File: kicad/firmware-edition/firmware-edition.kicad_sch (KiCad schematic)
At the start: 103 parts, among them J1 Solar Panel, J10 GPIO, J12 GPIO, J13 SPI, J2 BATT, J3 3V3 Sensor Bus, J4 USB_C_Receptacle_USB2.0_16P, J5 I2C_3V3, J6 SWD, J7 Conn_01x01_Socket, J8 GPIO, J9 I2C_5V, Q1 BSS84, Q2 BSS84, Q3 BSS84, SW1 BOOT_DFU, SW2 RST, U1 ADP5091, U2 TPS61023DRLR, U3 MAX-M10M-00B, U4 Si4463, U5 STM32U073KCU6, Y1 30MHz

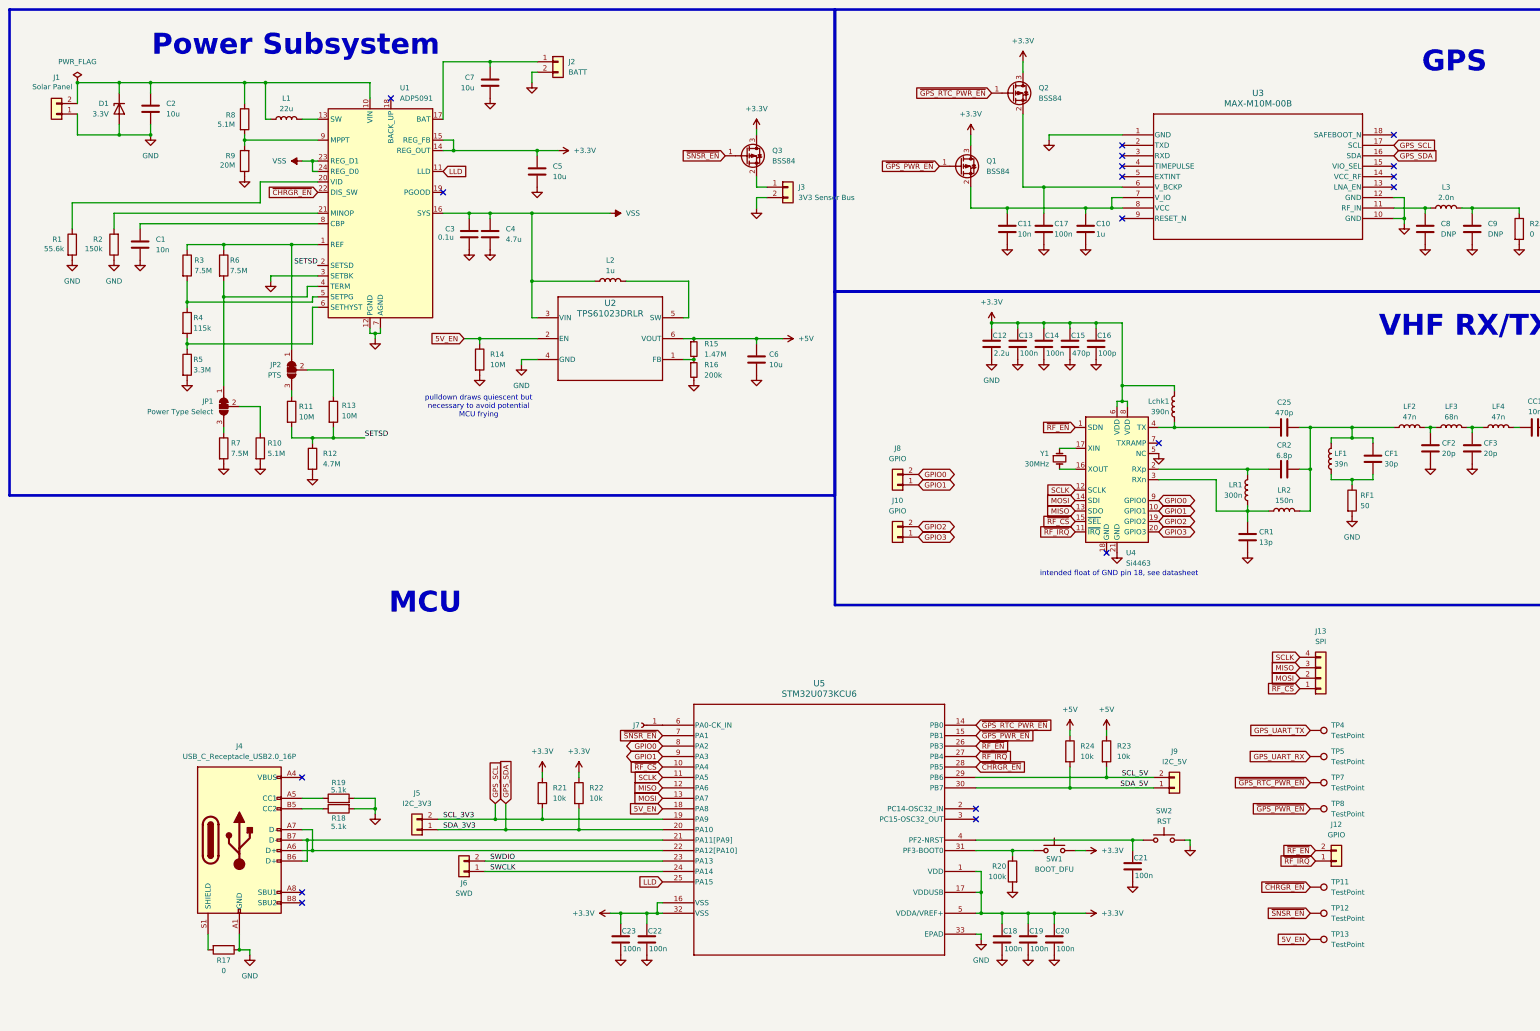
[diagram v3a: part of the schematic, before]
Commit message: PCB layout of System Board v1.01
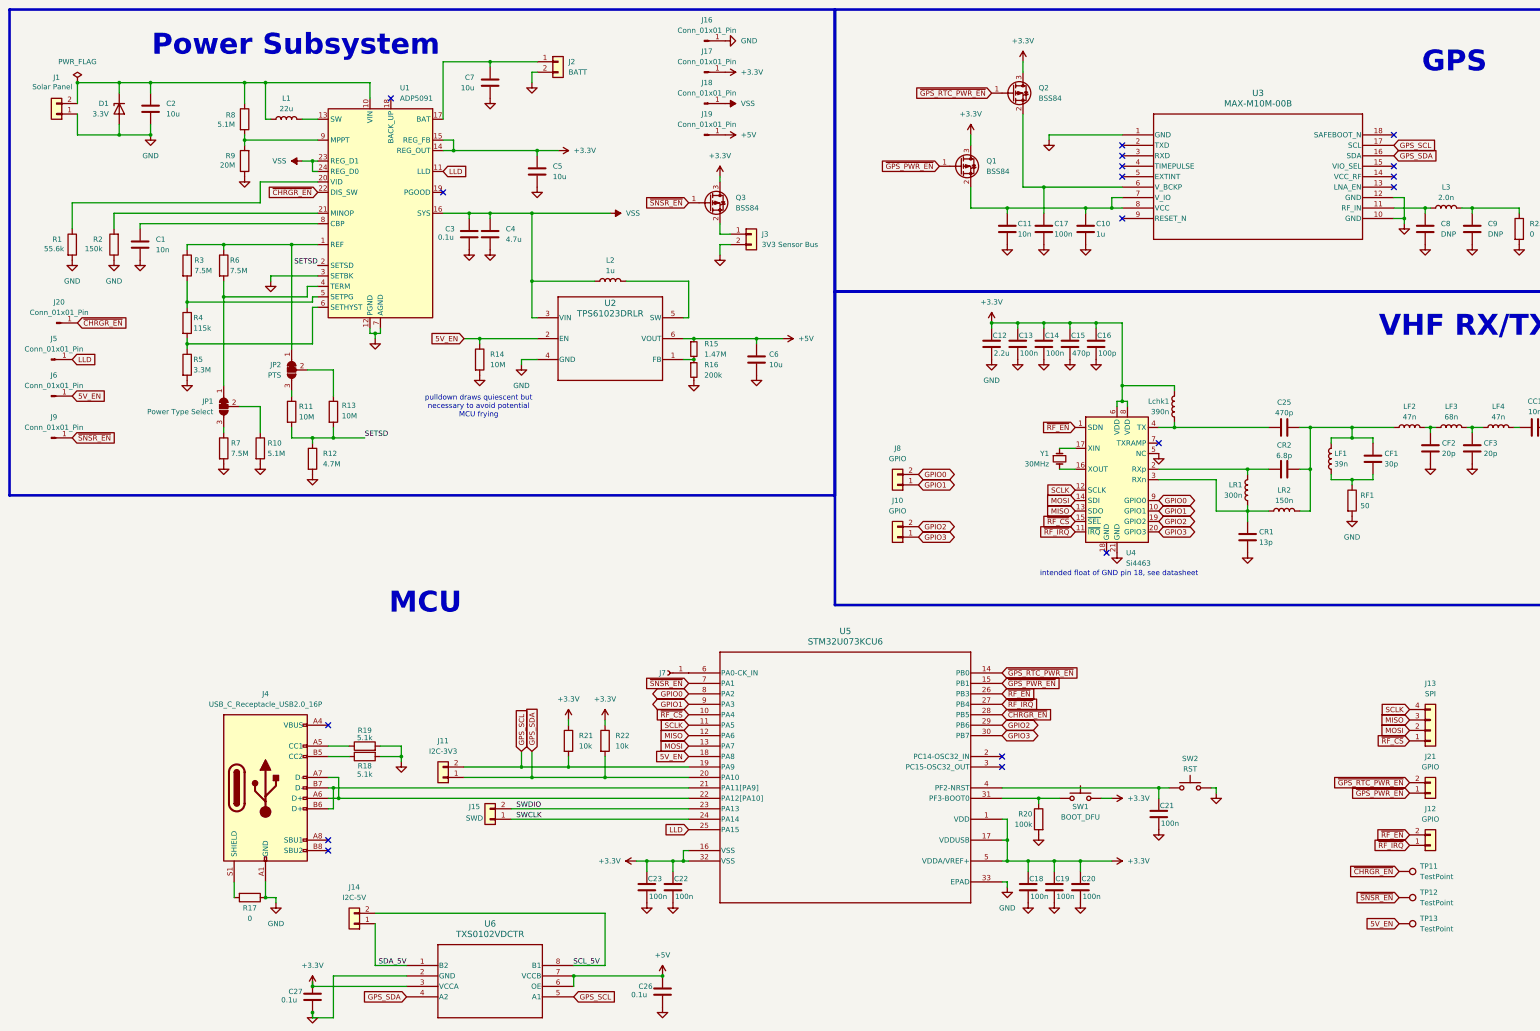
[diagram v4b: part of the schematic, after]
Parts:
- removed J5: I2C_3V3, symbol Connector_Generic:Conn_01x02
- removed J6: SWD, symbol Connector_Generic:Conn_01x02
- removed J9: I2C_5V, symbol Connector_Generic:Conn_01x02
- removed R23, R24: 10k, symbol Device:R
- removed TP4, TP5, TP7, TP8: TestPoint, symbol Connector:TestPoint
- added C26, C27: 0.1u, Capacitor_SMD:C_0603_1608Metric, symbol Device:C
- added J11: I2C-3V3, Connector_PinHeader_2.54mm:PinHeader_1x02_P2.54mm_Vertical, symbol Connector_Generic:Conn_01x02
- added J14: I2C-5V, Connector_PinHeader_2.54mm:PinHeader_1x02_P2.54mm_Vertical, symbol Connector_Generic:Conn_01x02
- added J15: SWD, Connector_PinHeader_2.54mm:PinHeader_1x02_P2.54mm_Vertical, symbol Connector_Generic:Conn_01x02
- added J16, J17, J18, J19, J20, J5, J6, J9: Conn_01x01_Pin, Connector_PinHeader_2.54mm:PinHeader_1x01_P2.54mm_Vertical, symbol Connector:Conn_01x01_Pin
- added J21: GPIO, Connector_PinHeader_2.54mm:PinHeader_1x02_P2.54mm_Vertical, symbol Connector_Generic:Conn_01x02
- added U6: TXS0102VDCTR, TXS0102V:SSOP8_DCT_TEX, symbol TXS0102V:TXS0102VDCTR
- AE1: footprint PicoAPRS-CustomFootprints:AC30157-01 GNSS Ceramic Chip -> Footprintsv2:AC30157-01 GNSS Ceramic Chip
- C10, C11, C17, C18, C19, C20, C21, C22, C23: footprint (none) -> Capacitor_SMD:C_0603_1608Metric
- J4: footprint (none) -> Connector_USB:USB_C_Receptacle_GCT_USB4105-xx-A_16P_TopMnt_Horizontal
- J7: footprint (none) -> Connector_PinHeader_1.00mm:PinHeader_1x01_P1.00mm_Vertical
- R17, R18, R19, R20, R21, R22: footprint (none) -> Resistor_SMD:R_0603_1608Metric
- RF1: footprint Resistor_SMD:R_0402_1005Metric -> Resistor_SMD:R_0603_1608Metric
- SW1, SW2: footprint (none) -> Button_Switch_SMD:Panasonic_EVQPUJ_EVQPUA
- TP11, TP12, TP13: footprint (none) -> TestPoint:TestPoint_Plated_Hole_D2.0mm
- U2: footprint DRL0006A -> TPS:DRL0006A
- U3: footprint MOD18_MAX-M10M_UBL -> Footprintsv2:MOD18_MAX-M10M_UBL
- U5: footprint UFQFPN-32_STM -> STM32073:UFQFPN-32_STM
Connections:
- net +3.3V: now also C27.1, J17.1 (Pin_1), U6.3 (VCCA)
- net +5V: now also C26.1, J19.1 (Pin_1), U6.6 (OE), U6.7 (VCCB)
- net 5V_EN: now also J6.1 (Pin_1)
- net GND: now also C26.2, C27.2, J16.1 (Pin_1), U6.2 (GND)
- net GPIO2: now also U5.29 (PB6)
- net GPIO3: now also U5.30 (PB7)
- net GPS_SCL: now also J11.2 (Pin_2), U6.5 (A1)
- net GPS_SDA: now also J11.1 (Pin_1), U6.4 (A2)
- net LLD: now also J5.1 (Pin_1)
- net SCL_5V: now also J14.2 (Pin_2), U6.8 (B1); no longer U5.29 (PB6)
- net SDA_5V: now also J14.1 (Pin_1), U6.1 (B2); no longer U5.30 (PB7)
- net SWCLK: now also J15.1 (Pin_1)
- net SWDIO: now also J15.2 (Pin_2)
- net VSS: now also J18.1 (Pin_1)
- net ~{CHRGR_EN}: now also J20.1 (Pin_1)
- net ~{GPS_PWR_EN}: now also J21.1 (Pin_1)
- net ~{GPS_RTC_PWR_EN}: now also J21.2 (Pin_2)
- net ~{SNSR_EN}: now also J9.1 (Pin_1)
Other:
- moved on the sheet: C18, C19, C20, C21, C22, C23, J12, J13, J3, J4, J7, Q3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

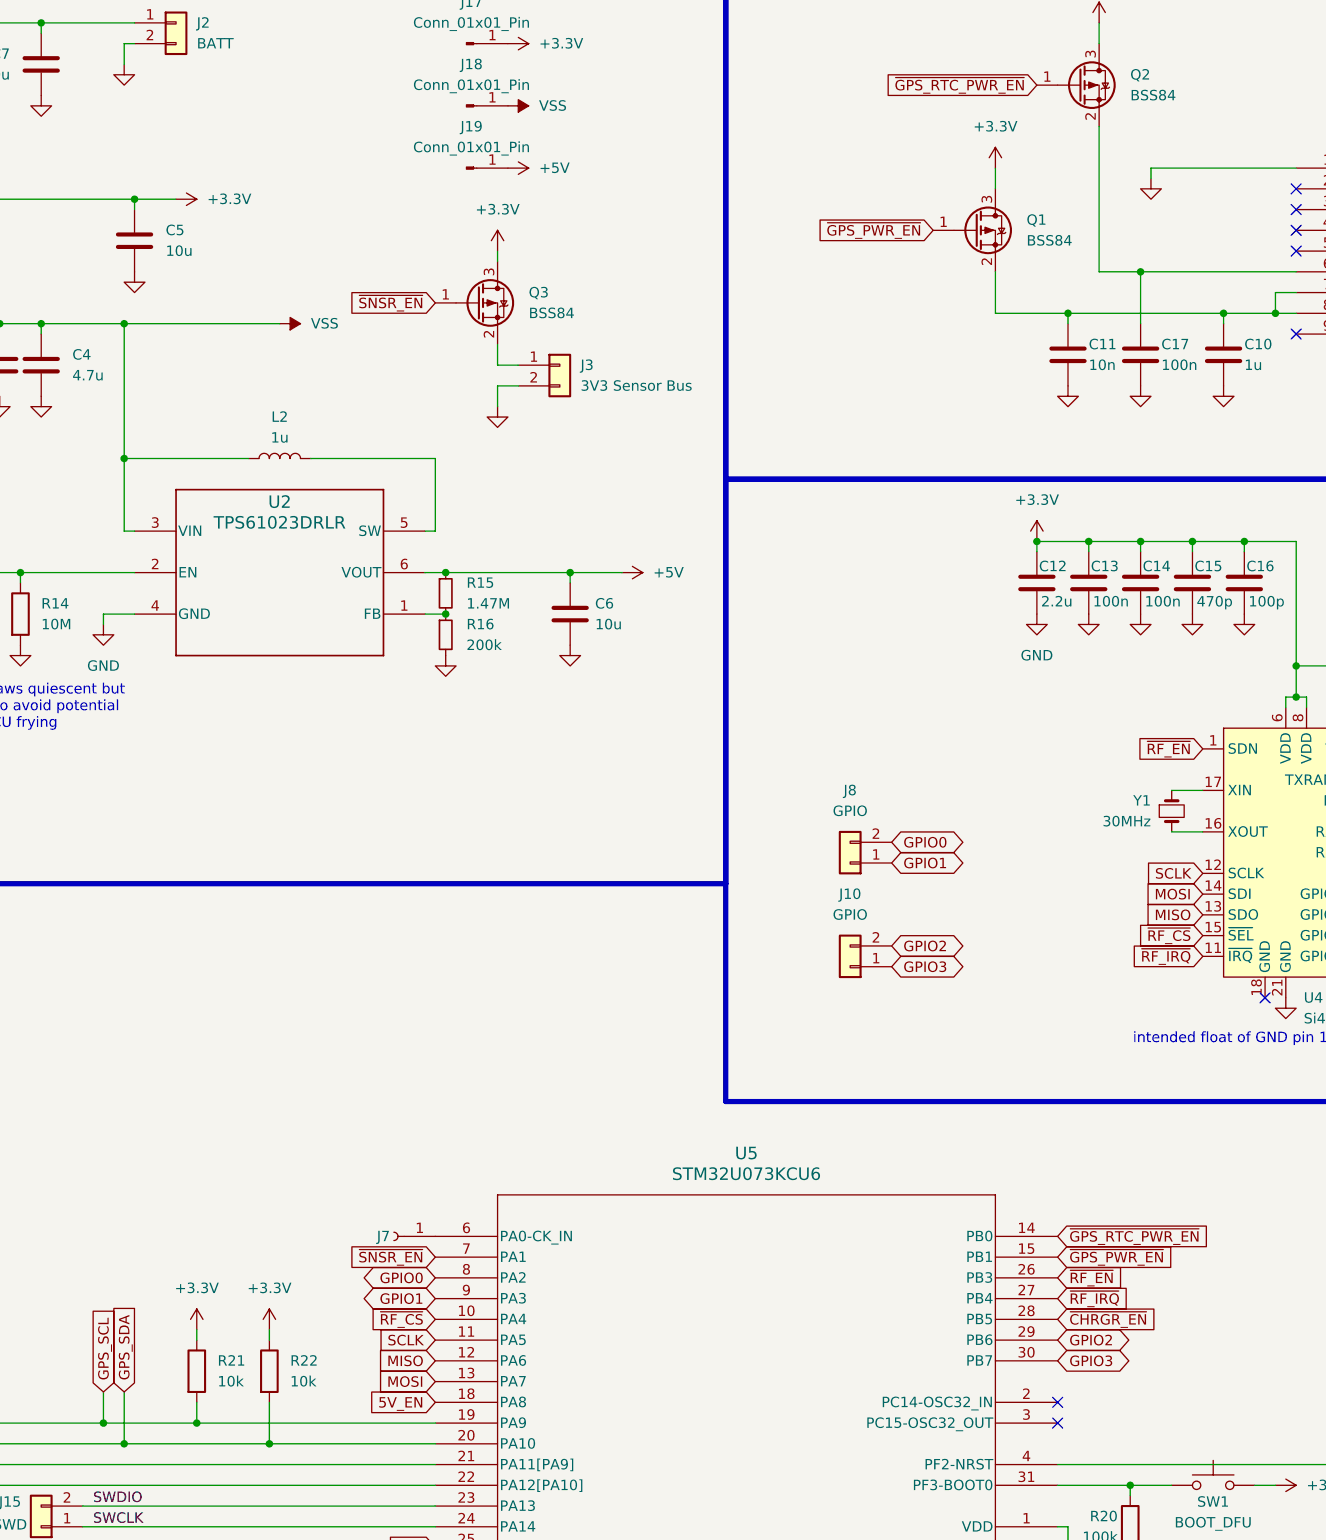
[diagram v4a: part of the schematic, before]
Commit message: Finished PCB layoiut of Integration board V1.01
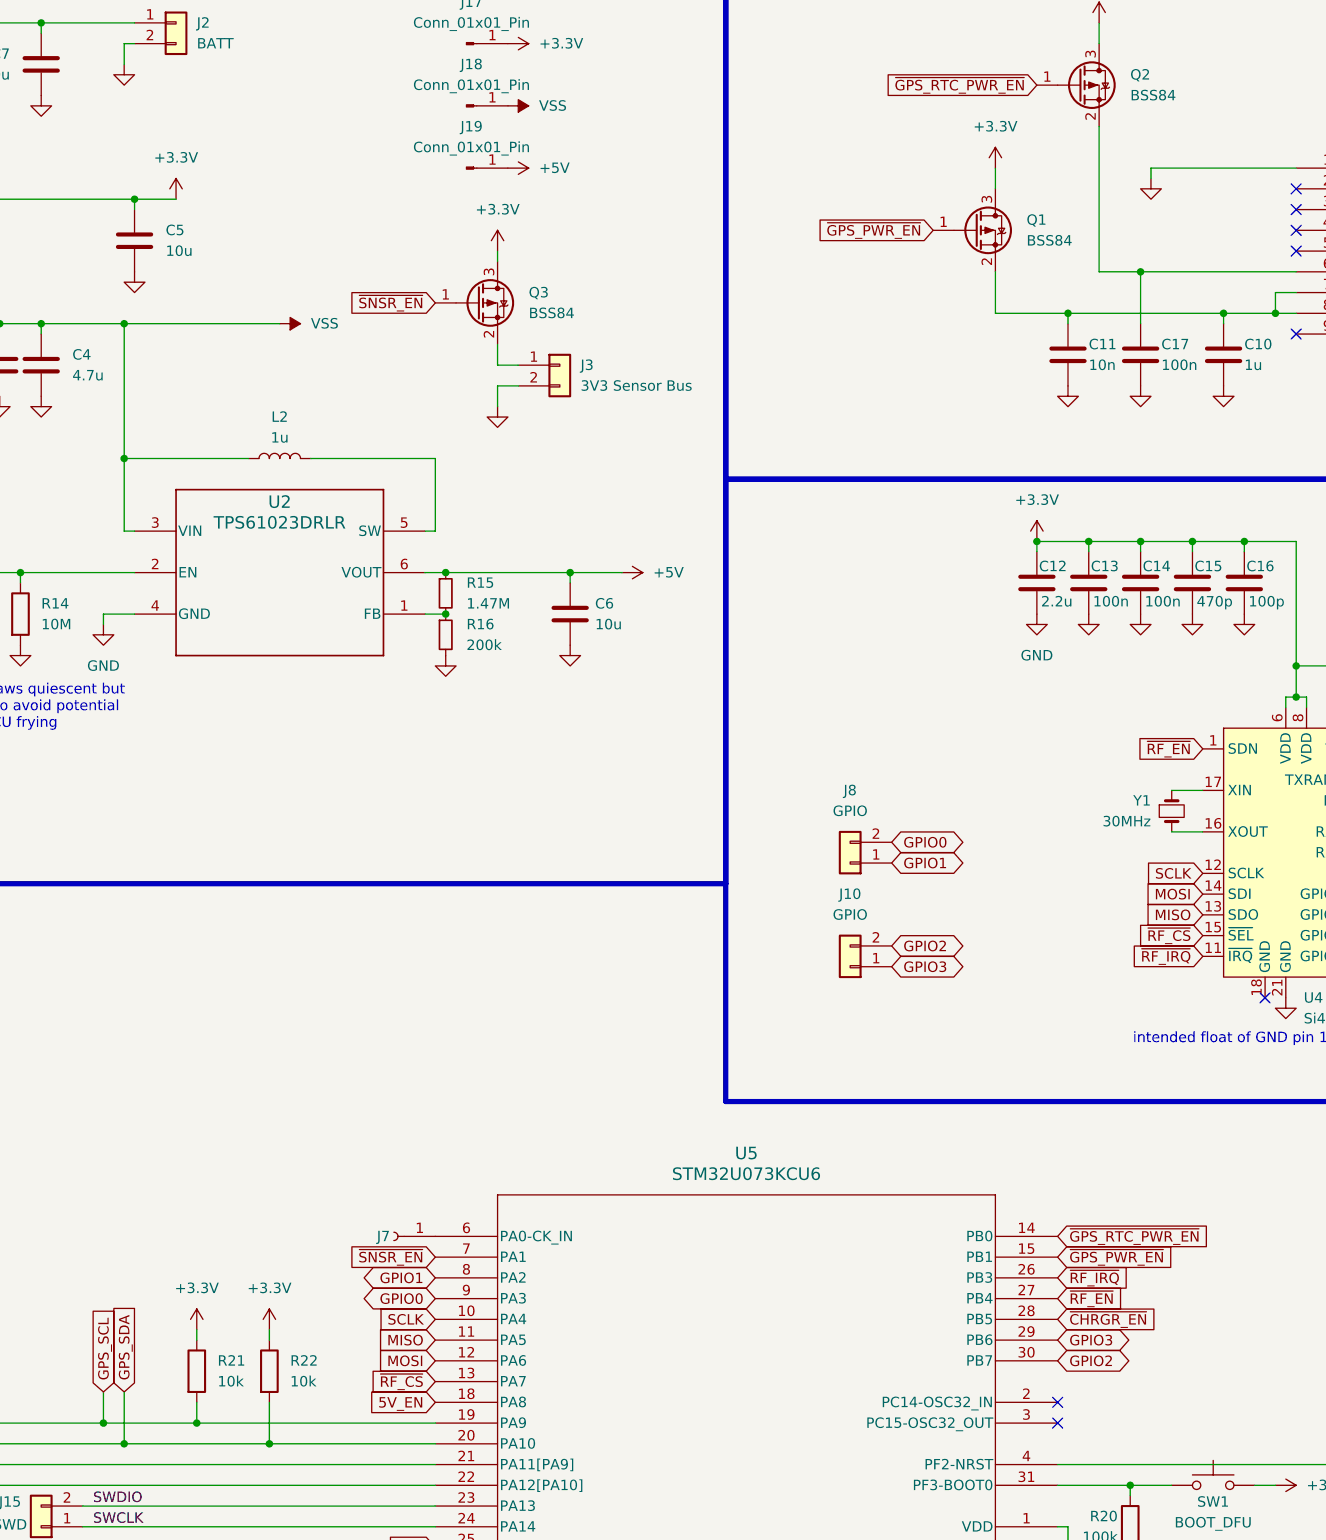
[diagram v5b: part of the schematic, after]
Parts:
- J16: footprint Connector_PinHeader_2.54mm:PinHeader_1x01_P2.54mm_Vertical -> Connector_PinHeader_2.54mm:PinHeader_1x02_P2.54mm_Vertical
- TP11, TP12, TP13: footprint TestPoint:TestPoint_Plated_Hole_D2.0mm -> Connector_PinHeader_1.00mm:PinHeader_1x01_P1.00mm_Vertical
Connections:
- net GPIO0: now also U5.9 (PA3); no longer U5.8 (PA2)
- net GPIO1: now also U5.8 (PA2); no longer U5.9 (PA3)
- net GPIO2: now also U5.30 (PB7); no longer U5.29 (PB6)
- net GPIO3: now also U5.29 (PB6); no longer U5.30 (PB7)
- net MISO: now also U5.11 (PA5); no longer U5.12 (PA6)
- net MOSI: now also U5.12 (PA6); no longer U5.13 (PA7)
- net SCLK: now also U5.10 (PA4); no longer U5.11 (PA5)
- net ~{RF_CS}: now also U5.13 (PA7); no longer U5.10 (PA4)
- net ~{RF_EN}: now also U5.27 (PB4); no longer U5.26 (PB3)
- net ~{RF_IRQ}: now also U5.26 (PB3); no longer U5.27 (PB4)
